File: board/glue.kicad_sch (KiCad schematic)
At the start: 7 parts, among them J1 Conn_01x05_Pin, U12 GLUE

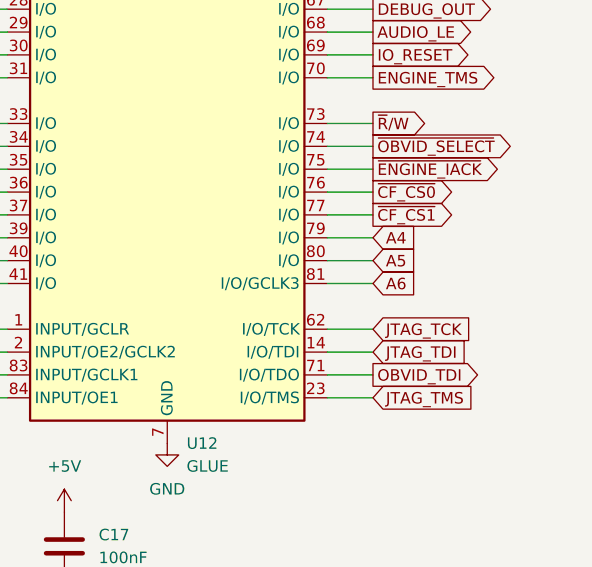
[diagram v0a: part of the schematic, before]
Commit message: JTAG bypass, GLUE A18, OBVID pins
Fix up JTAG bypass again
Switch GLUE A6 to GLUE A18
Clean up some OBVID pins
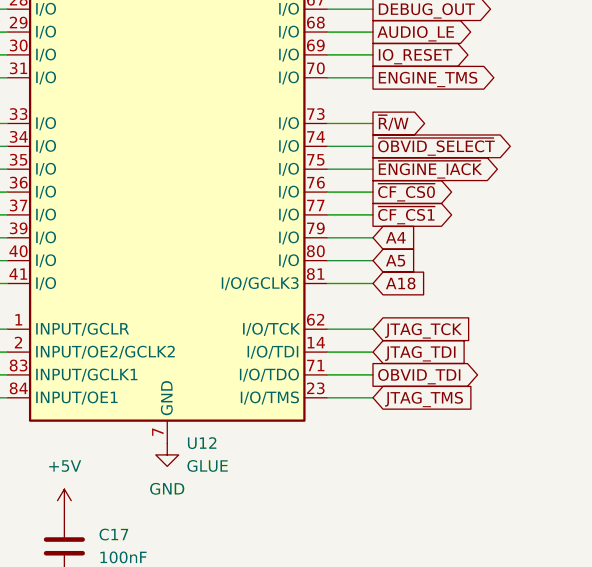
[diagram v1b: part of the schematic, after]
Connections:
- net A6 renamed A18
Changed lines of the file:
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@@
 		)
 	)
-	(global_label "A6"
+	(global_label "A18"
 		(shape input)
 		(at 118.11 156.21 0)
@@
 		)
 		(property "Intersheetrefs" "${INTERSHEET_REFS}"
-			(at 123.3933 156.21 0)
+			(at 124.6028 156.21 0)
 			(effects
 				(font

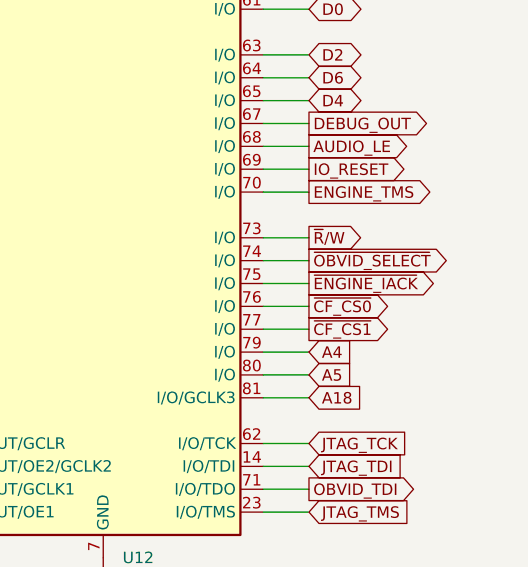
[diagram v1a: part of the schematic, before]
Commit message: Run VPA from GLUE to CPU
* delete old ENGINE_IACK line and pullup - interrupts will be autovectored
* run VPA between GLUE and CPU
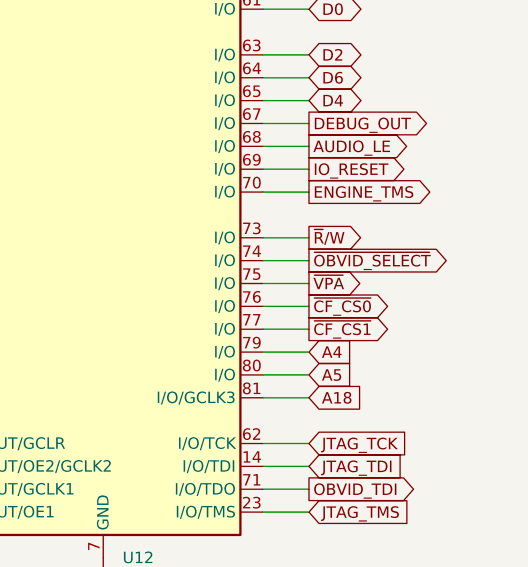
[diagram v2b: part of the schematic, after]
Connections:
- net ~{ENGINE_IACK} renamed ~{VPA}
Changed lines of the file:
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@@
 		)
 	)
-	(global_label "~{ENGINE_IACK}"
+	(global_label "~{VPA}"
 		(shape output)
 		(at 118.11 143.51 0)
@@
 		)
 		(property "Intersheetrefs" "${INTERSHEET_REFS}"
-			(at 133.13 143.51 0)
+			(at 124.5424 143.51 0)
 			(effects
 				(font

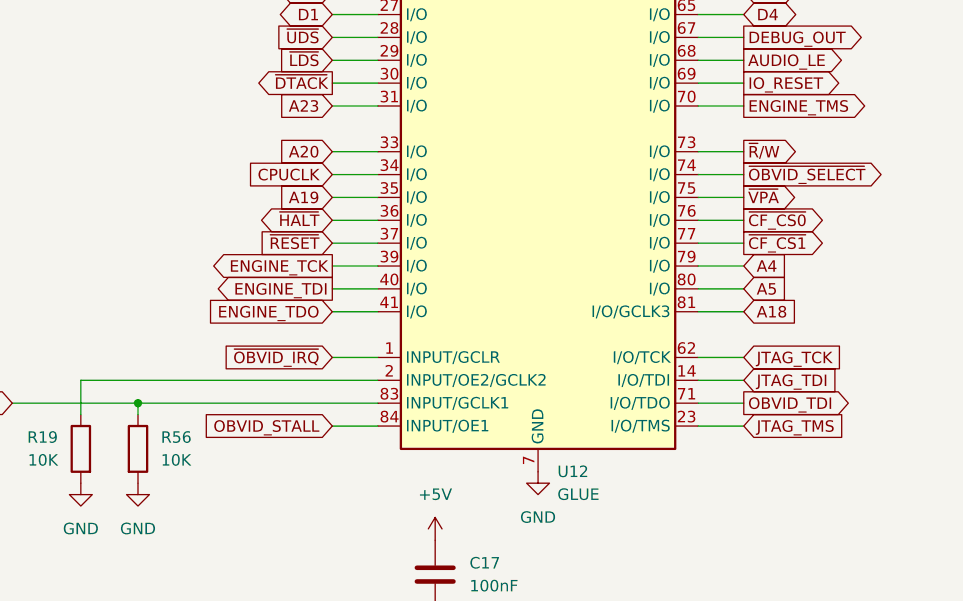
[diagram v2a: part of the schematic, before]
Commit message: change OBVID to VIDEO
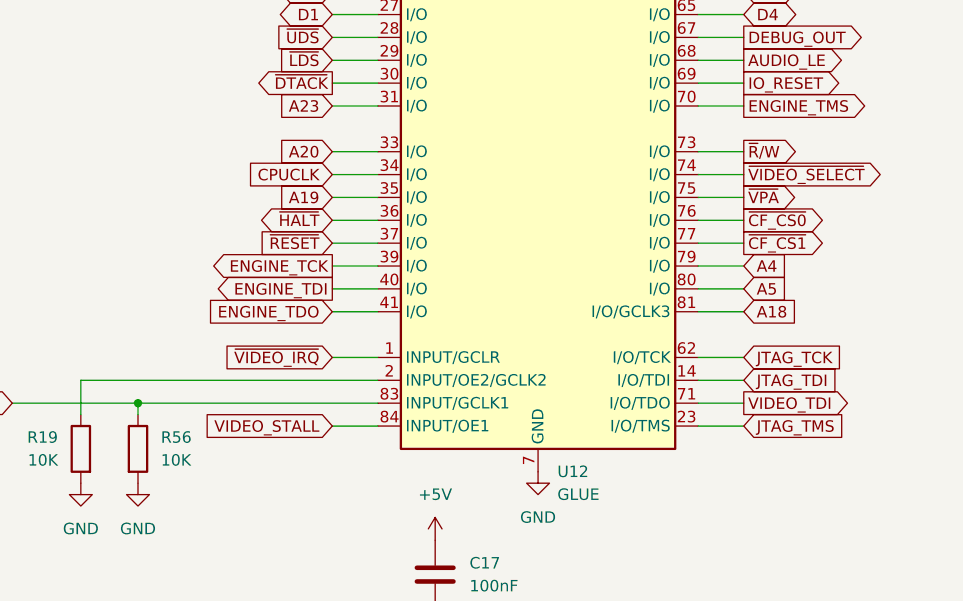
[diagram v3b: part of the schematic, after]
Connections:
- net OBVID_STALL renamed VIDEO_STALL
- net OBVID_TDI renamed VIDEO_TDI
- net ~{OBVID_IRQ} renamed ~{VIDEO_IRQ}
- net ~{OBVID_SELECT} renamed ~{VIDEO_SELECT}
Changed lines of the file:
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@@
 		)
 	)
-	(global_label "OBVID_STALL"
+	(global_label "VIDEO_STALL"
 		(shape input)
 		(at 72.39 168.91 180)
@@
 		)
 	)
-	(global_label "OBVID_TDI"
+	(global_label "VIDEO_TDI"
 		(shape output)
 		(at 118.11 166.37 0)
@@
 		)
 	)
-	(global_label "~{OBVID_SELECT}"
+	(global_label "~{VIDEO_SELECT}"
 		(shape output)
 		(at 118.11 140.97 0)
@@
 		)
 	)
-	(global_label "~{OBVID_IRQ}"
+	(global_label "~{VIDEO_IRQ}"
 		(shape input)
 		(at 72.39 161.29 180)

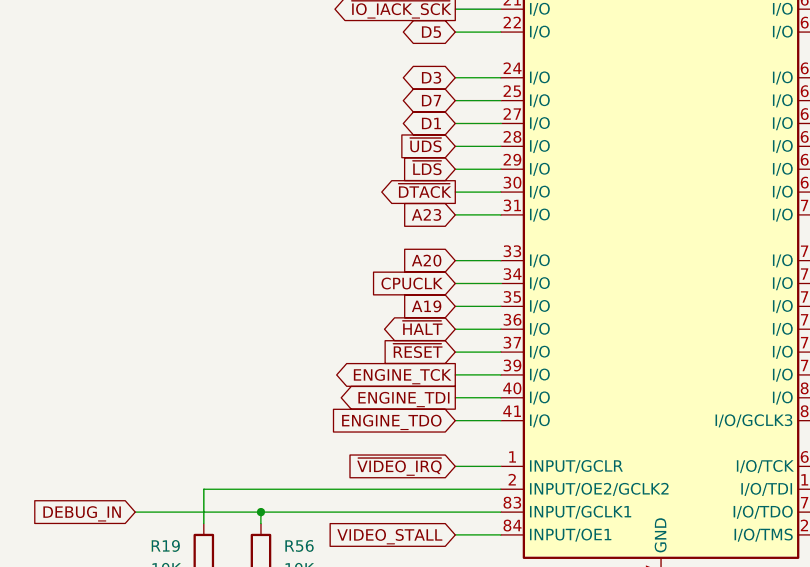
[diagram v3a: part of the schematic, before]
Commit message: CPUCLK -> SYSCLK
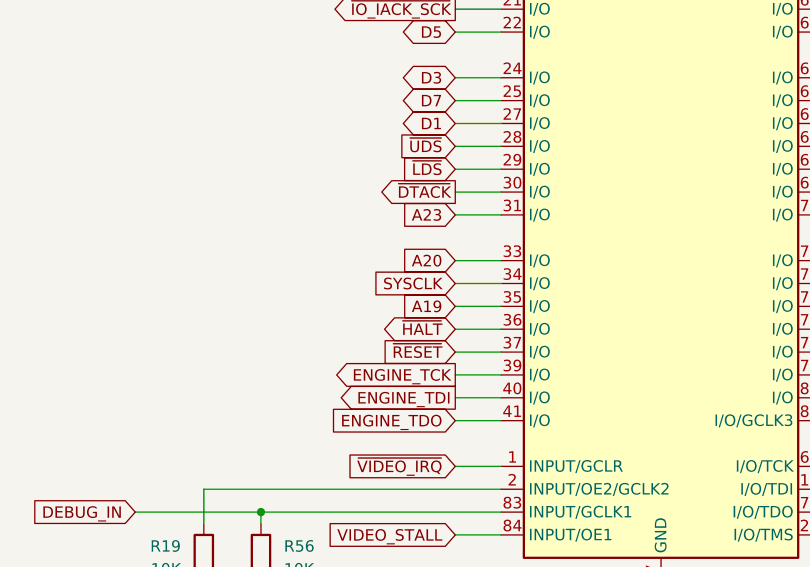
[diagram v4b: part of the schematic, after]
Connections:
- net CPUCLK renamed SYSCLK
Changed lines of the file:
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@@
 		)
 	)
-	(global_label "CPUCLK"
+	(global_label "SYSCLK"
 		(shape input)
 		(at 72.39 140.97 180)

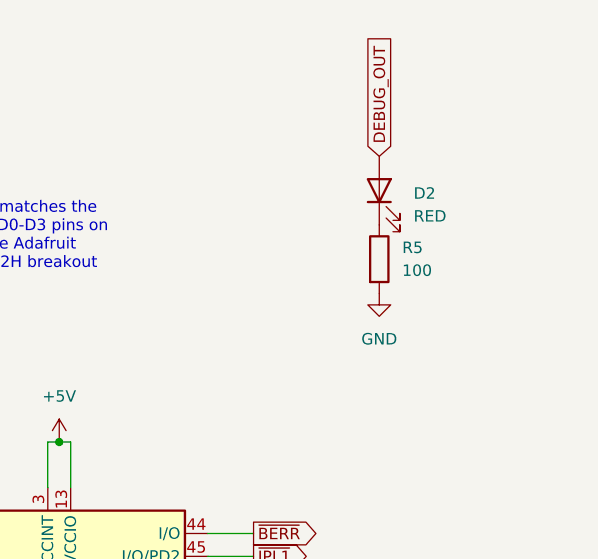
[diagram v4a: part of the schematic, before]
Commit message: add DEBUG_OUT LED driver to isolate from logic
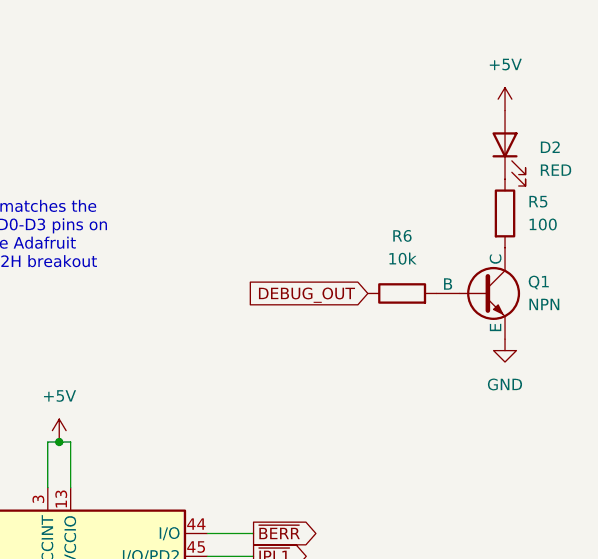
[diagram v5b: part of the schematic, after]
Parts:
- added Q1: NPN, Package_TO_SOT_THT:TO-92, symbol Simulation_SPICE:NPN
- added R6: 10k, Resistor_THT:R_Axial_DIN0207_L6.3mm_D2.5mm_P10.16mm_Horizontal, symbol Device:R
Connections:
- net +5V: now also D2.2 (A)
- net DEBUG_OUT: now also R6.1; no longer D2.2 (A)
- net GND: now also Q1.3 (E); no longer R5.2
- new net: Q1.2 (B), R6.2
- new net: Q1.1 (C), R5.2
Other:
- moved on the sheet: D2, R5

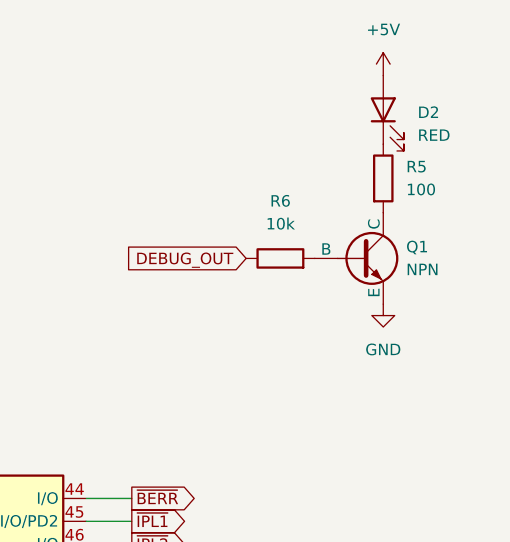
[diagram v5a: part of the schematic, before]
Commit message: use correct symbol and footprint for 2222
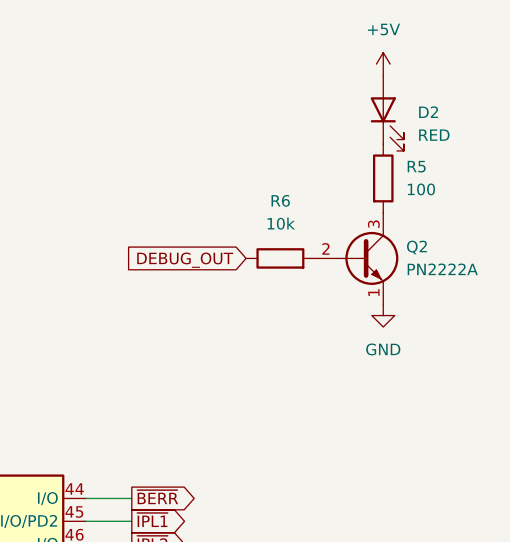
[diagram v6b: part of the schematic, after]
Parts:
- removed Q1: NPN, Package_TO_SOT_THT:TO-92, symbol Simulation_SPICE:NPN
- added Q2: PN2222A, Package_TO_SOT_THT:TO-92_Inline, symbol Transistor_BJT:PN2222A
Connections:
- net GND: now also Q2.1 (E)
- net at R6.2: now also Q2.2 (B)
- net at R5.2: now also Q2.3 (C)
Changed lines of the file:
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@@
 	)
 	(symbol
-		(lib_id "Simulation_SPICE:NPN")
+		(lib_id "Transistor_BJT:PN2222A")
 		(at 143.51 48.26 0)
 		(unit 1)
@@
 		(dnp no)
 		(fields_autoplaced yes)
-		(property "Reference" "Q1"
+		(property "Reference" "Q2"
 			(at 148.59 46.9899 0)
 			(effects
@@
 			)
 		)
-		(property "Value" "NPN"
+		(property "Value" "PN2222A"
 			(at 148.59 49.5299 0)
 			(effects
@@
 			)
 		)
-		(property "Footprint" "Package_TO_SOT_THT:TO-92"
-			(at 207.01 48.26 0)
+		(property "Footprint" "Package_TO_SOT_THT:TO-92_Inline"
+			(at 148.59 50.165 0)
+			(effects
+				(font
+					(size 1.27 1.27)
+					(italic yes)
+				)
+				(justify left)
+				(hide yes)
+			)
+		)
+		(property "Datasheet" "https://www.onsemi.com/pub/Collateral/PN2222-D.PDF"
+			(at 143.51 48.26 0)
 			(effects
 				(font
 					(size 1.27 1.27)
 				)
+				(justify left)
 				(hide yes)
 			)
 		)
-		(property "Datasheet" "https://ngspice.sourceforge.io/docs/ngspice-html-manual/manual.xhtml#cha_BJTs"
-			(at 207.01 48.26 0)
-			(effects
-				(font
-					(size 1.27 1.27)
-				)
-				(hide yes)
-			)
-		)
-		(property "Description" "Bipolar transistor symbol for simulation only, substrate tied to the emitter"
+		(property "Description" "1A Ic, 40V Vce, NPN Transistor, General Purpose Transistor, TO-92"
 			(at 143.51 48.26 0)
 			(effects
@@
 			)
 		)
-		(property "Sim.Type" "GUMMELPOON"
+		(property "Sim.Pins" "1=E 2=B 3=C"
 			(at 143.51 48.26 0)
 			(effects
@@
 			)
 		)
-		(property "Sim.Pins" "1=C 2=B 3=E"
-			(at 143.51 48.26 0)
-			(effects
-				(font
-					(size 1.27 1.27)
-				)
-				(hide yes)
-			)
-		)
-		(pin "2"
-		)
 		(pin "1"
 		)
 		(pin "3"
 		)
+		(pin "2"
+		)
 		(instances
 			(project ""
 				(path "/afefa398-9f39-4b22-97f8-dae9b102df0d/04c090b1-601c-4801-ba2d-bdadcdd34cff"
-					(reference "Q1")
+					(reference "Q2")
 					(unit 1)
 				)
